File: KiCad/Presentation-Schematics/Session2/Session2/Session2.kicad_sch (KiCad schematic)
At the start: 3 parts, among them U1 ESP32-WROOM-32

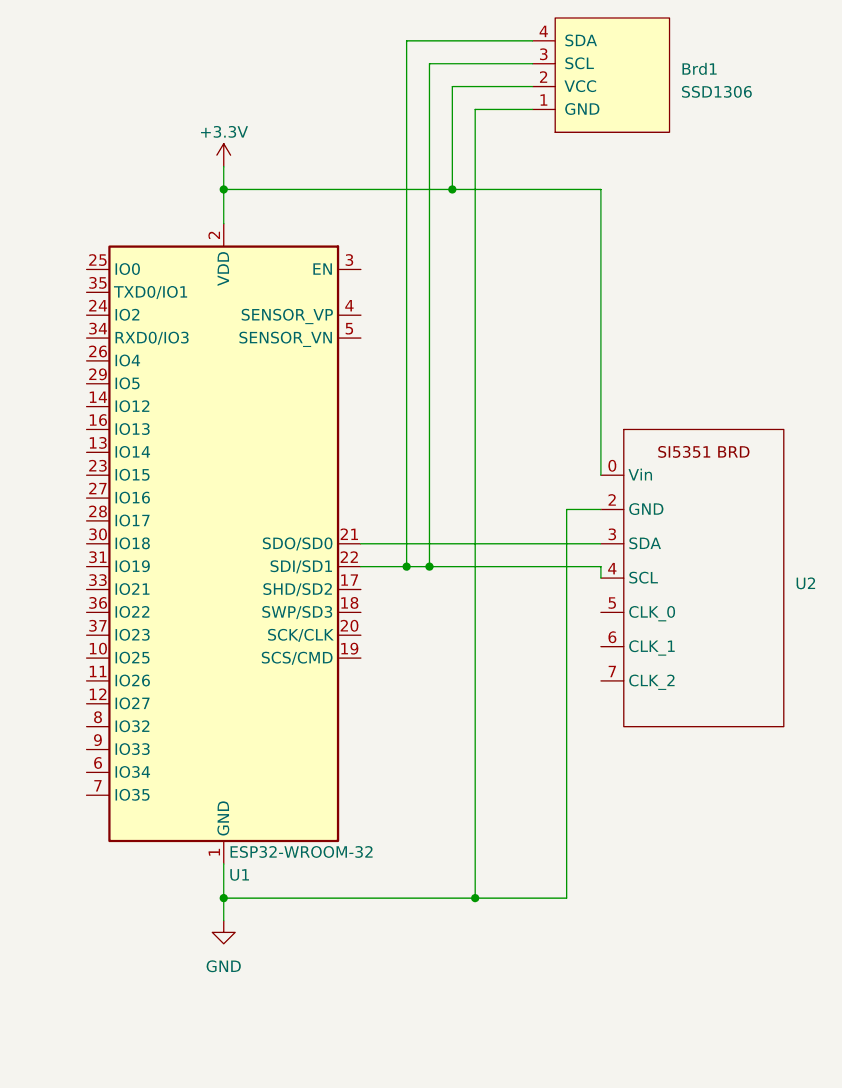
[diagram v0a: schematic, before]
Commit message: revert code to pre presentation
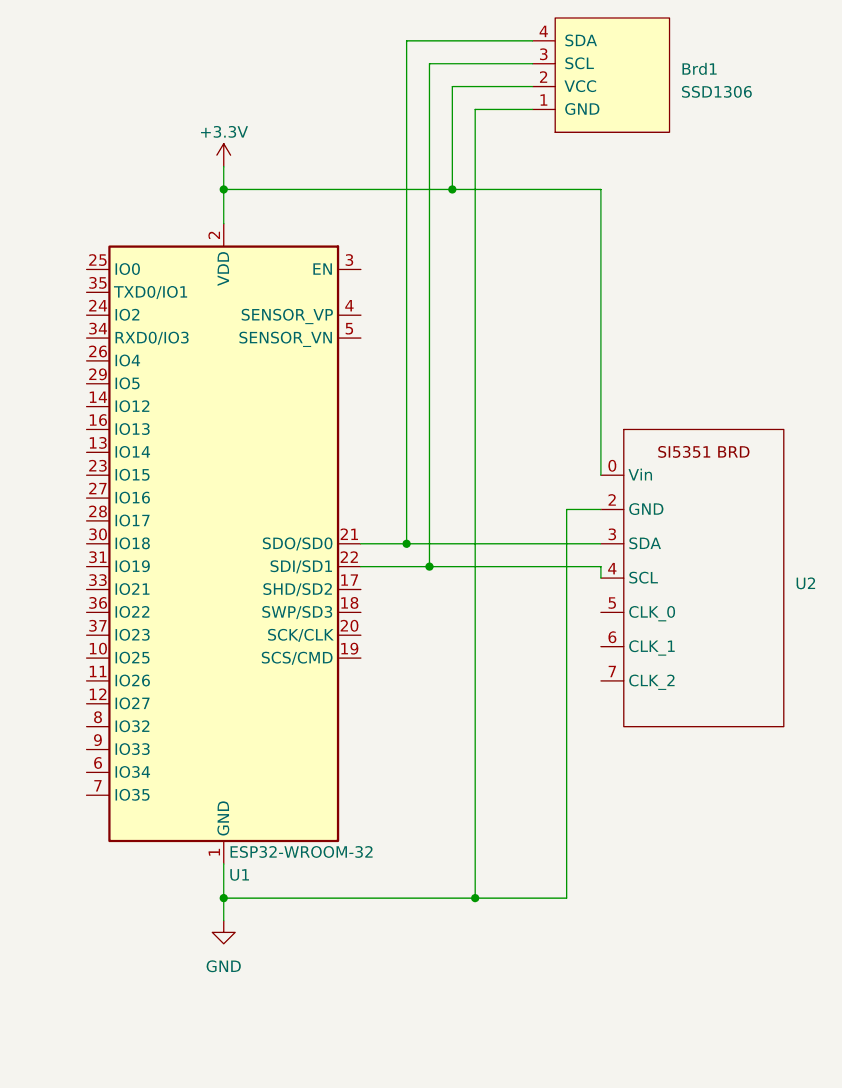
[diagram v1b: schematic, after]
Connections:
- net at Brd1.3 (SCL), U1.22 (SDI/SD1), U2.4 (SCL): no longer Brd1.4 (SDA)
- net at U1.21 (SDO/SD0), U2.3 (SDA): now also Brd1.4 (SDA)
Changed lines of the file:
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@@
   (junction (at 109.22 43.18) (diameter 0) (color 0 0 0 0)
   )
+  (junction (at 104.14 82.55) (diameter 0) (color 0 0 0 0)
+  )
   (junction (at 83.82 121.92) (diameter 0) (color 0 0 0 0)
-  )
-  (junction (at 104.14 85.09) (diameter 0) (color 0 0 0 0)
   )
   (junction (at 106.68 85.09) (diameter 0) (color 0 0 0 0)
@@
     (stroke (width 0) (type default))
   )
-  (wire (pts (xy 99.06 82.55) (xy 125.73 82.55))
+  (wire (pts (xy 99.06 82.55) (xy 104.14 82.55))
     (stroke (width 0) (type default))
   )
@@
     (stroke (width 0) (type default))
   )
-  (wire (pts (xy 104.14 26.67) (xy 104.14 85.09))
-    (stroke (width 0) (type default))
-  )
   (wire (pts (xy 125.73 78.74) (xy 121.92 78.74))
     (stroke (width 0) (type default))
@@
     (stroke (width 0) (type default))
   )
+  (wire (pts (xy 104.14 26.67) (xy 104.14 82.55))
+    (stroke (width 0) (type default))
+  )
   (wire (pts (xy 83.82 43.18) (xy 83.82 46.99))
     (stroke (width 0) (type default))
   )
-  (wire (pts (xy 104.14 85.09) (xy 106.68 85.09))
+  (wire (pts (xy 99.06 85.09) (xy 106.68 85.09))
+    (stroke (width 0) (type default))
+  )
+  (wire (pts (xy 104.14 82.55) (xy 125.73 82.55))
     (stroke (width 0) (type default))
   )
@@
     (stroke (width 0) (type default))
   )
-  (wire (pts (xy 99.06 85.09) (xy 104.14 85.09))
-    (stroke (width 0) (type default))
-  )

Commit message: updates for session 4
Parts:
- added SW1: ~, symbol ILoveHamRadio:Rotary Encoder
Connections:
- net +3.3V: now also SW1.2 (VCC)
- net GND: now also SW1.1 (GND)
- net at U1.18 (SWP/SD3): now also SW1.4 (DT)
- net at U1.19 (SCS/CMD): now also SW1.3 (SW)
- net at U1.29 (IO5): now also SW1.5 (CLK)
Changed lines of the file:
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@@
   (junction (at 111.76 121.92) (diameter 0) (color 0 0 0 0)
+  )
+  (junction (at 111.76 118.11) (diameter 0) (color 0 0 0 0)
+  )
+  (junction (at 116.84 43.18) (diameter 0) (color 0 0 0 0)
   )
   (junction (at 83.82 43.18) (diameter 0) (color 0 0 0 0)
   )
-  (wire (pts (xy 125.73 43.18) (xy 109.22 43.18))
+  (wire (pts (xy 125.73 43.18) (xy 116.84 43.18))
+    (stroke (width 0) (type default))
+  )
+  (wire (pts (xy 60.96 137.16) (xy 60.96 64.77))
     (stroke (width 0) (type default))
   )
@@
     (stroke (width 0) (type default))
   )
+  (wire (pts (xy 127 128.27) (xy 99.06 128.27))
+    (stroke (width 0) (type default))
+  )
   (wire (pts (xy 118.11 29.21) (xy 106.68 29.21))
+    (stroke (width 0) (type default))
+  )
+  (wire (pts (xy 116.84 123.19) (xy 116.84 43.18))
+    (stroke (width 0) (type default))
+  )
+  (wire (pts (xy 99.06 128.27) (xy 99.06 95.25))
     (stroke (width 0) (type default))
   )
@@
     (stroke (width 0) (type default))
   )
+  (wire (pts (xy 127 133.35) (xy 105.41 133.35))
+    (stroke (width 0) (type default))
+  )
   (wire (pts (xy 109.22 43.18) (xy 83.82 43.18))
+    (stroke (width 0) (type default))
+  )
+  (wire (pts (xy 127 123.19) (xy 116.84 123.19))
+    (stroke (width 0) (type default))
+  )
+  (wire (pts (xy 105.41 133.35) (xy 105.41 90.17))
     (stroke (width 0) (type default))
   )
@@
     (stroke (width 0) (type default))
   )
-  (wire (pts (xy 111.76 34.29) (xy 111.76 121.92))
+  (wire (pts (xy 111.76 34.29) (xy 111.76 118.11))
     (stroke (width 0) (type default))
   )
@@
     (stroke (width 0) (type default))
   )
-  (wire (pts (xy 121.92 121.92) (xy 111.76 121.92))
+  (wire (pts (xy 111.76 121.92) (xy 121.92 121.92))
     (stroke (width 0) (type default))
   )
@@
     (stroke (width 0) (type default))
   )
+  (wire (pts (xy 105.41 90.17) (xy 99.06 90.17))
+    (stroke (width 0) (type default))
+  )
   (wire (pts (xy 118.11 31.75) (xy 109.22 31.75))
     (stroke (width 0) (type default))
   )
   (wire (pts (xy 106.68 85.09) (xy 125.73 85.09))
+    (stroke (width 0) (type default))
+  )
+  (wire (pts (xy 60.96 64.77) (xy 68.58 64.77))
+    (stroke (width 0) (type default))
+  )
+  (wire (pts (xy 127 137.16) (xy 60.96 137.16))
+    (stroke (width 0) (type default))
+  )
+  (wire (pts (xy 111.76 118.11) (xy 111.76 121.92))
+    (stroke (width 0) (type default))
+  )
+  (wire (pts (xy 116.84 43.18) (xy 109.22 43.18))
+    (stroke (width 0) (type default))
+  )
+  (wire (pts (xy 111.76 118.11) (xy 127 118.11))
     (stroke (width 0) (type default))
   )
@@
     (stroke (width 0) (type default))
   )
+  (symbol (lib_id "ILoveHamRadio:Rotary Encoder") (at 137.16 128.27 0) (unit 1)
+    (in_bom yes) (on_board yes) (dnp no) (fields_autoplaced)
+    (property "Reference" "SW1" (at 144.78 128.27 0)
+      (effects (font (size 1.27 1.27)) (justify left))
+    )
+    (property "Value" "~" (at 137.16 128.27 0)
+      (effects (font (size 1.27 1.27)))
+    )
+    (property "Footprint" "" (at 137.16 128.27 0)
+      (effects (font (size 1.27 1.27)) hide)
+    )
+    (property "Datasheet" "" (at 137.16 128.27 0)
+      (effects (font (size 1.27 1.27)) hide)
+    )
+    (pin "1")
+    (pin "2")
+    (pin "3")
+    (pin "4")
+    (pin "5")
+    (instances
+      (project "Session2"
+        (path "/478282aa-0889-4707-af51-1bc3ea02c993"
+          (reference "SW1") (unit 1)
+        )
+      )
+    )
+  )
   (symbol (lib_id "SSD1306-128x64_OLED:SSD1306") (at 127 30.48 90) (unit 1)
